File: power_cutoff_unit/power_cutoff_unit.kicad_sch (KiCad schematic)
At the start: 13 parts, among them J1 Conn_01x02, J2 Conn_01x02, K2 T9GS1L14-5, Q1 AO3400A, SW1 SW_DIP_x02, U1 MOUDLE-SEEEDUINO-XIAO-ESP32C3, U2 STM32G431K8Tx

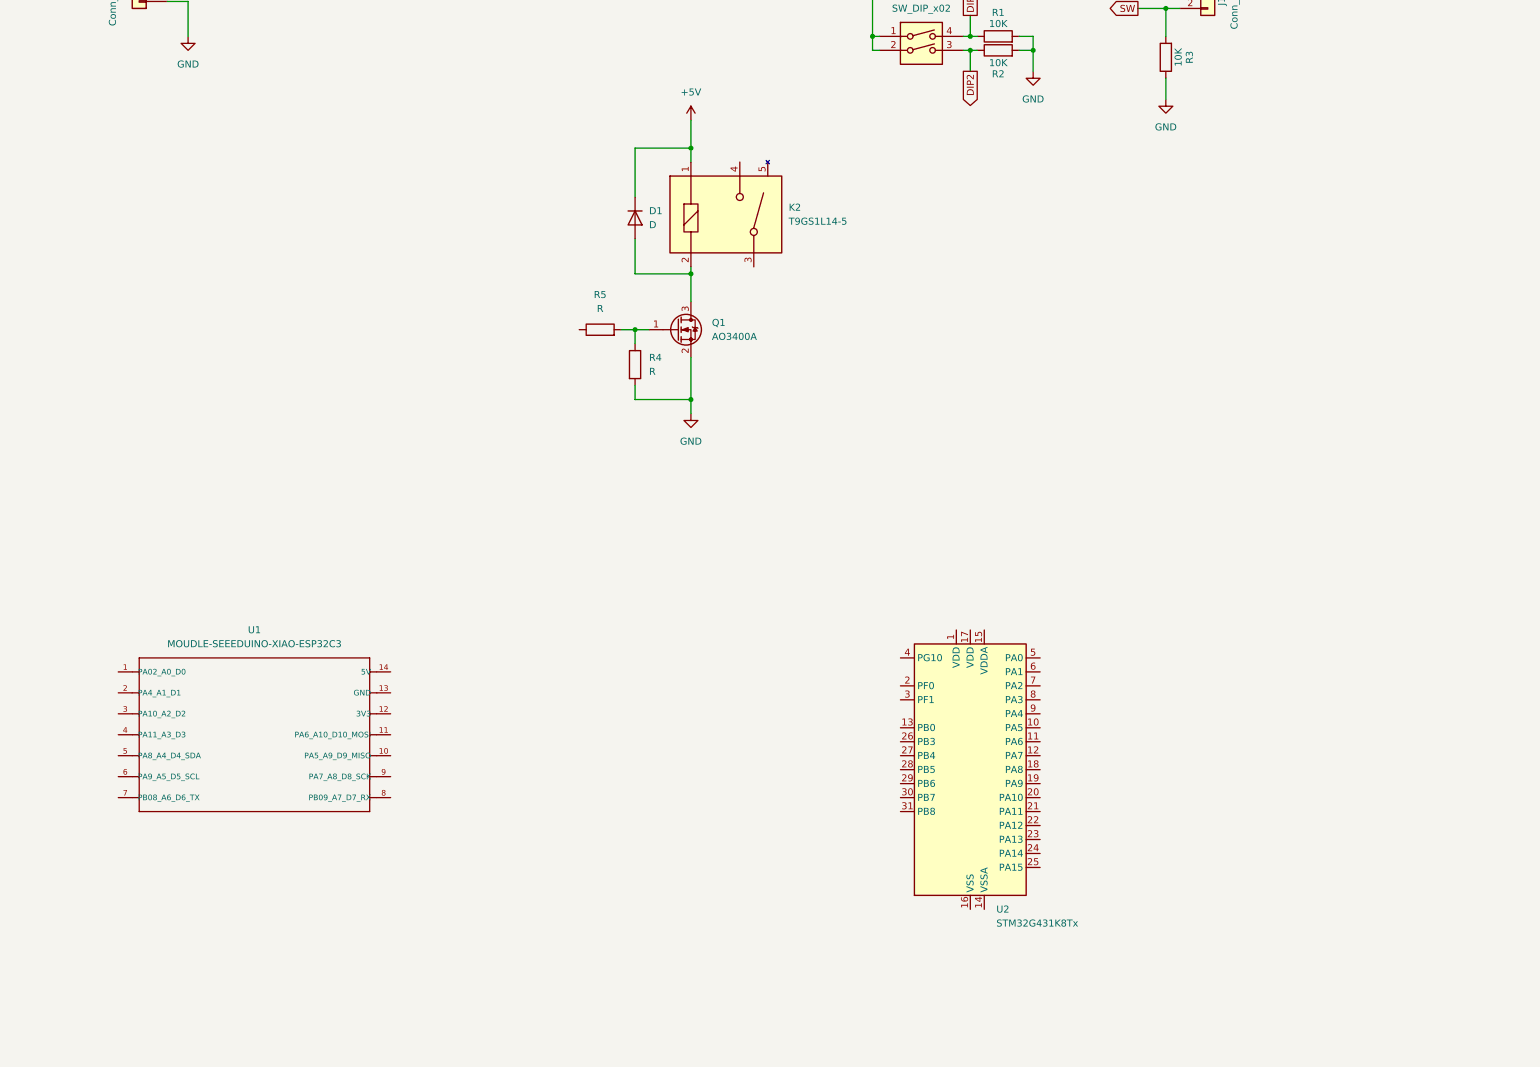
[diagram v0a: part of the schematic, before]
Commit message: 駆動系側の電圧変換ICを追加した
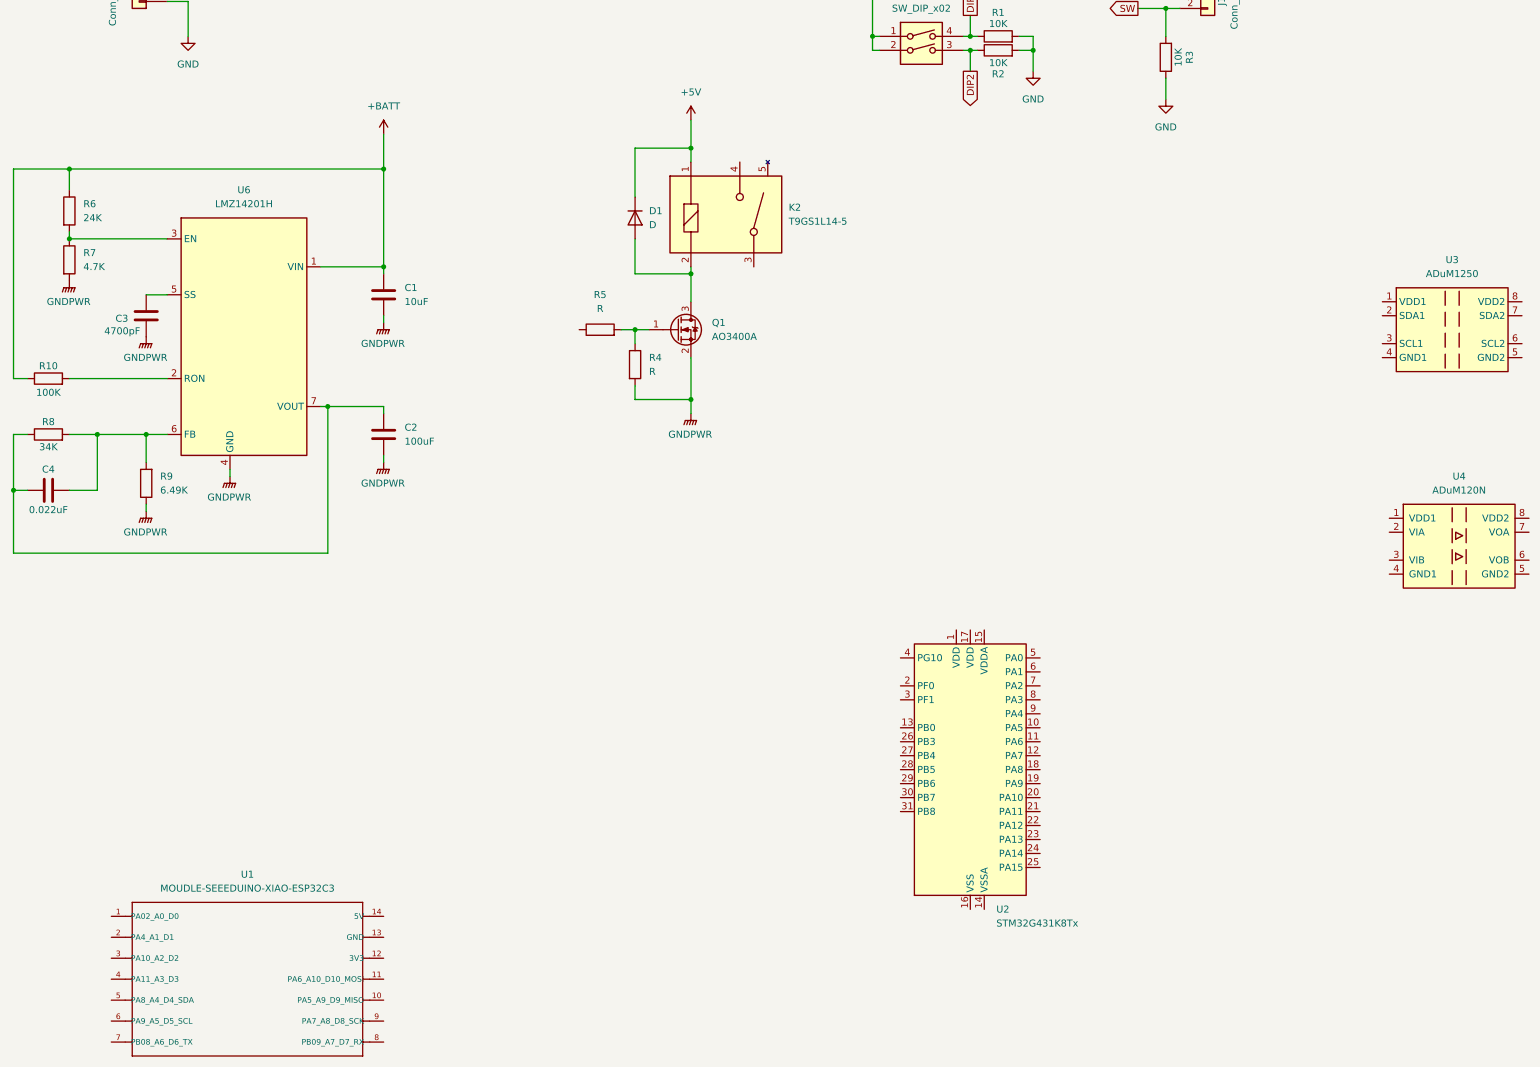
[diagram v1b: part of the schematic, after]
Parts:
- added C1: 10uF, symbol Device:C
- added C2: 100uF, symbol Device:C
- added C3: 4700pF, symbol Device:C
- added C4: 0.022uF, symbol Device:C
- added R10: 100K, symbol Device:R
- added R6: 24K, symbol Device:R
- added R7: 4.7K, symbol Device:R
- added R8: 34K, symbol Device:R
- added R9: 6.49K, symbol Device:R
- added U3: ADuM1250, Package_SO:SOIC-8_3.9x4.9mm_P1.27mm, symbol Isolator:ADuM1250
- added U4: ADuM120N, Package_SO:SOIC-8_3.9x4.9mm_P1.27mm, symbol Isolator:ADuM120N
- added U6: LMZ14201H, symbol LMZ14201H:LMZ14201H
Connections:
- net GND: no longer Q1.2 (S), R4.2
- new net: R10.2, U6.2 (RON)
- new net: R6.2, R7.1, U6.3 (EN)
- new net: C2.1, C4.1, R8.1, U6.7 (VOUT)
- new net: C4.2, R8.2, R9.2, U6.6 (FB)
- new net: C3.1, U6.5 (SS)
- new net +BATT: C1.1, R10.1, R6.1, U6.1 (VIN)
- new net GNDPWR: C1.2, C2.2, C3.2, Q1.2 (S), R4.2, R7.2, R9.1, U6.4 (GND)
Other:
- moved on the sheet: U1

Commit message: 難しくてわかんないッピ
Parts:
- removed U1: MOUDLE-SEEEDUINO-XIAO-ESP32C3, MOUDLE14P-SMD-2.54-21X17.8MM, symbol MOUDLE-SEEEDUINO-XIAO-ESP32C3:MOUDLE-SEEEDUINO-XIAO-ESP32C3
- removed U4: ADuM120N, Package_SO:SOIC-8_3.9x4.9mm_P1.27mm, symbol Isolator:ADuM120N
- added U5: ADuM263N, Package_SO:SOIC-16W_7.5x12.8mm_P1.27mm, symbol Isolator:ADuM263N
- R4: value R -> 20K
- R5: value R -> 470
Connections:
- net +5V is gone; now on net VDD: D1.1 (K), K2.1
- net VDD: now reaches C2.1, C4.1, R8.1, U6.7 (VOUT)
- net RELAY_EN: now reaches R5.1
- net RELAY_EN: now also U5.15 (VOA)
- new net DISCHARGE: U5.14 (VOB)
- new net INDICATOR: U5.13 (VOC)
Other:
- moved on the sheet: C1, C2, C3, C4, D1, J1, J2, K2, Q1, R1, R10, R2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

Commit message: 尽きた
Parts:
- removed U5: ADuM263N, Package_SO:SOIC-16W_7.5x12.8mm_P1.27mm, symbol Isolator:ADuM263N
- added J3, J4, J5: Conn_01x02, Connector_JST:JST_XH_S2B-XH-A_1x02_P2.50mm_Horizontal, symbol Connector_Generic:Conn_01x02
- added R11, R12: 10K, Resistor_SMD:R_0603_1608Metric, symbol Device:R
- added U1: ADuM120N, Package_SO:SOIC-8_3.9x4.9mm_P1.27mm, symbol Isolator:ADuM120N
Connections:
- net +3.3V: now also U3.1 (VDD1), J3.1 (Pin_1), J4.1 (Pin_1), U1.1 (VDD1)
- net DISCHARGE: now also U1.6 (VOB)
- net GND: now also U3.4 (GND1), J5.2 (Pin_2), R11.1, R12.1, U1.4 (GND1)
- net GNDPWR: now also U3.5 (GND2), U1.5 (GND2)
- net RELAY_EN: now also U1.7 (VOA)
- net VDD: now also U3.8 (VDD2), U1.8 (VDD2)
- net SW renamed SW_1
- new net ENABLE: J5.1 (Pin_1)
- new net SW_2: J3.2 (Pin_2), R11.2
- new net SW_3: J4.2 (Pin_2), R12.2
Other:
- moved on the sheet: J1, R1, R2, R3, SW1, U2, U3

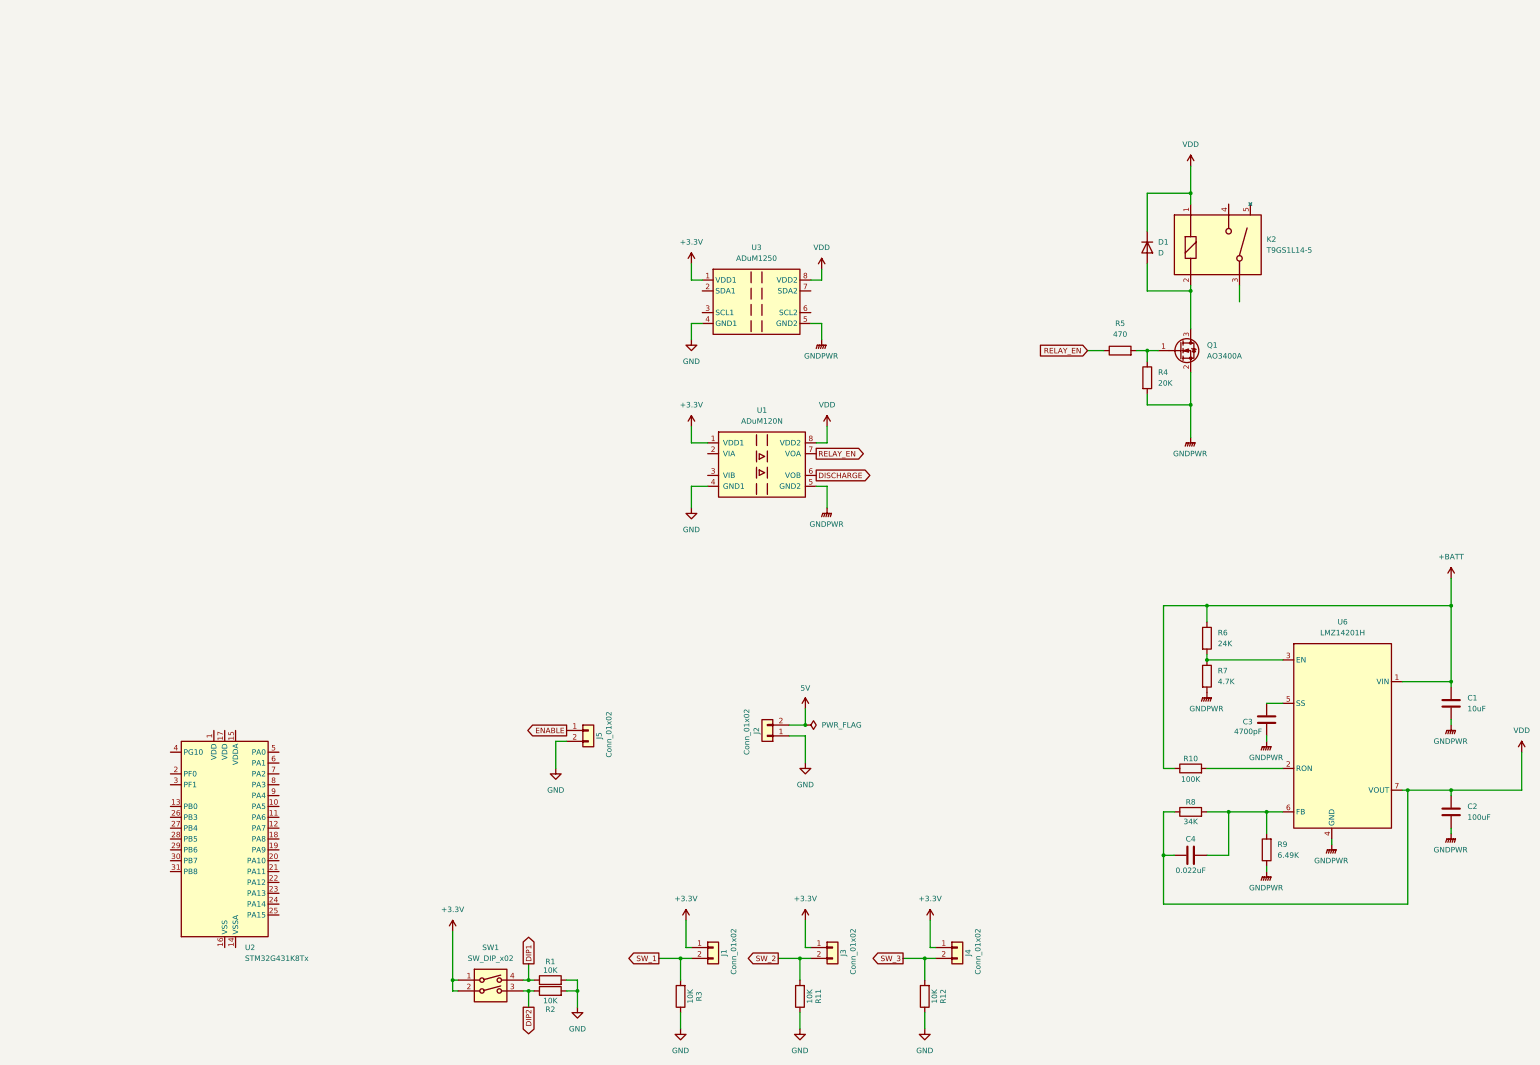
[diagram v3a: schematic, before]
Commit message: 細かい部品追加した。
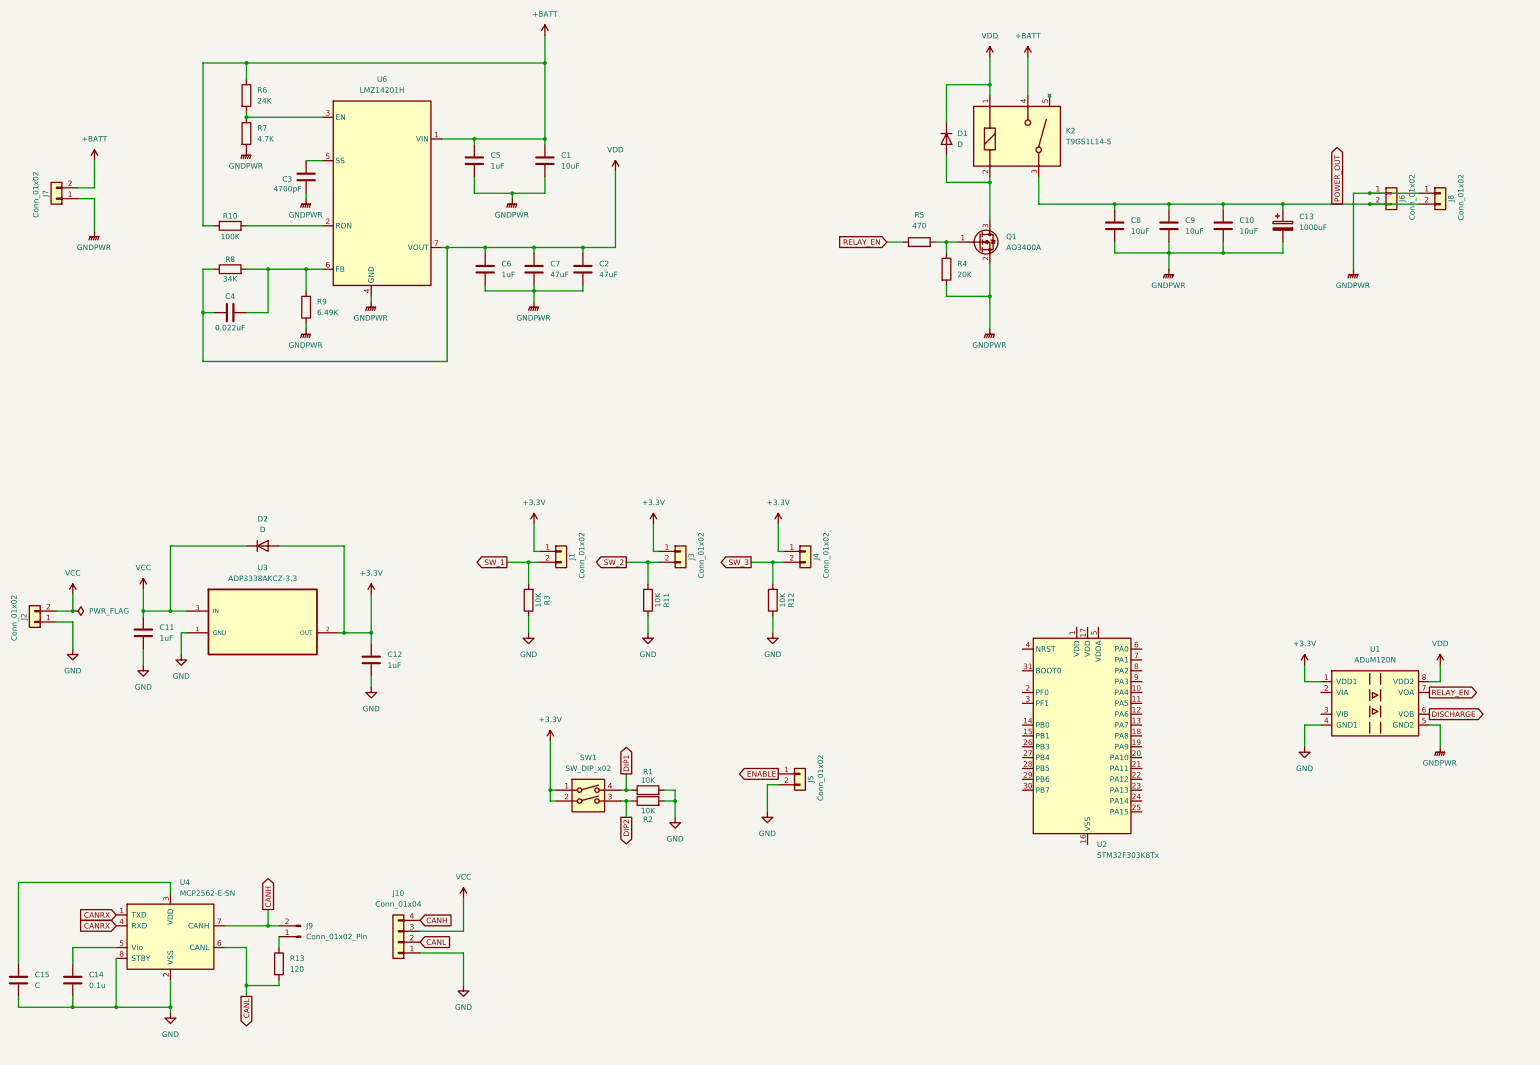
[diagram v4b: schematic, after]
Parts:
- removed U2: STM32G431K8Tx, Package_QFP:LQFP-32_7x7mm_P0.8mm, symbol MCU_ST_STM32G4:STM32G431K8Tx
- removed U3: ADuM1250, Package_SO:SOIC-8_3.9x4.9mm_P1.27mm, symbol Isolator:ADuM1250
- added C10, C8, C9: 10uF, symbol Device:C
- added C11, C12, C5, C6: 1uF, symbol Device:C
- added C13: 1000uF, symbol Device:C_Polarized
- added C14: 0.1u, symbol Device:C
- added C15: C, symbol Device:C
- added C7: 47uF, symbol Device:C
- added D2: D, symbol Device:D
- added J10: Conn_01x04, symbol Connector_Generic:Conn_01x04
- added J6, J7, J8: Conn_01x02, Connector_AMASS:AMASS_XT30PW-M_1x02_P2.50mm_Horizontal, symbol Connector_Generic:Conn_01x02
- added J9: Conn_01x02_Pin, symbol Connector:Conn_01x02_Pin
- added R13: 120, symbol Device:R
- added U2: STM32F303K8Tx, Package_QFP:LQFP-32_7x7mm_P0.8mm, symbol MCU_ST_STM32F3:STM32F303K8Tx
- added U3: ADP3338AKCZ-3.3, SOT230P700X180-4N, symbol 0_symbols:ADP3338AKCZ-3.3
- added U4: MCP2562-E-SN, Package_SO:SOIC-8_3.9x4.9mm_P1.27mm, symbol Interface_CAN_LIN:MCP2562-E-SN
- C2: value 100uF -> 47uF
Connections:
- net +3.3V: now also C12.1, D2.2 (A), U3.2 (OUT)
- net +BATT: now also K2.4, C5.1, J7.2 (Pin_2)
- net GND: now also C11.2, C12.2, C14.2, C15.2, J10.1 (Pin_1), U3.1 (GND), U4.2 (VSS), U4.8 (STBY)
- net GNDPWR: now also C10.2, C13.2, C5.2, C6.2, C7.2, C8.2, C9.2, J6.1 (Pin_1), J7.1 (Pin_1), J8.1 (Pin_1)
- net VDD: now also C6.1, C7.1
- net POWER_OUT: now reaches K2.3
- net POWER_OUT: now also C10.1, C13.1, C8.1, C9.1, J6.2 (Pin_2), J8.2 (Pin_2)
- net 5V renamed VCC
- net VCC: now also C11.1, D2.1 (K), J10.3 (Pin_3), U3.3 (IN)
- new net: C15.1, U4.3 (VDD)
- new net: C14.1, U4.5 (Vio)
- new net: J9.1 (Pin_1), R13.1
- new net: U2.16 (VSS), U2.32 (VSS)
- new net CANH: J10.4 (Pin_4), J9.2 (Pin_2), U4.7 (CANH)
- new net CANL: J10.2 (Pin_2), R13.2, U4.6 (CANL)
- new net CANRX: U4.1 (TXD), U4.4 (RXD)
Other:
- moved on the sheet: C1, C2, C3, C4, D1, J1, J2, J3, J4, J5, K2, Q1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
